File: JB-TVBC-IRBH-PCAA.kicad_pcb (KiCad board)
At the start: 2 copper layers, 65 x 56 mm, 11 parts, among them J1 CONN_2x20_FEM_100PITCH_635INS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, U1 CAT24C32

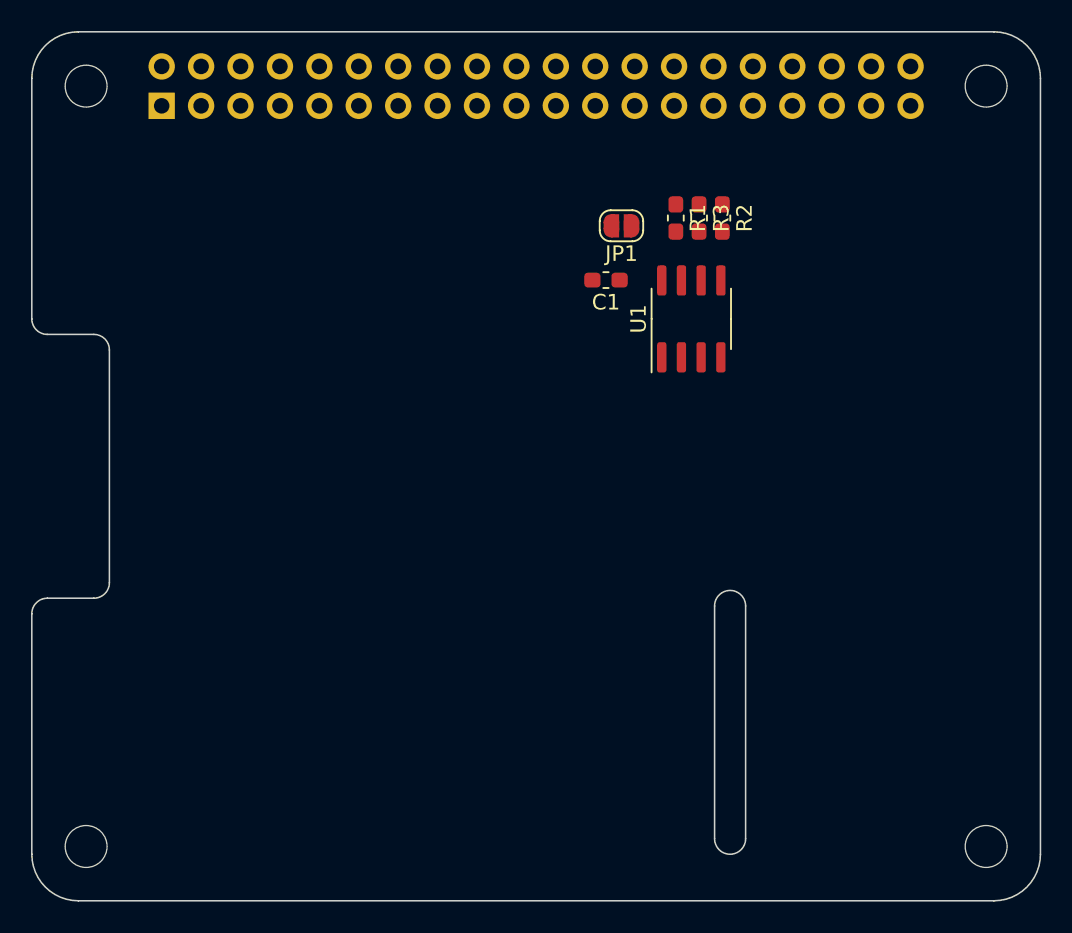
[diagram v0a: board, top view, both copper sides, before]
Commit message: WIP. need to remove pull-up on PHASE and add pull-down on IN (gate driver
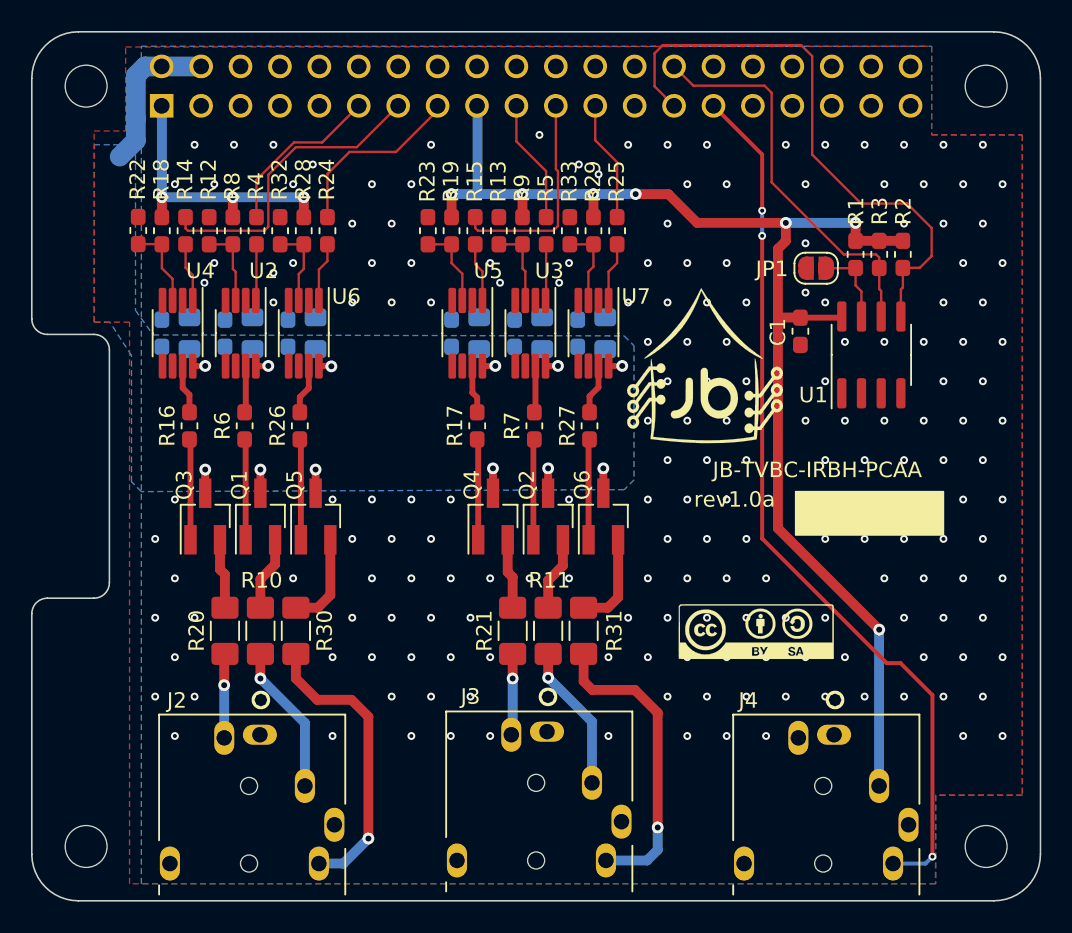
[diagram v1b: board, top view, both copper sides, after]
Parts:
- added C10: 4.7uF_CER_0805_16V, Capacitor_SMD:C_0805_2012Metric_Pad1.15x1.40mm_HandSolder, B.Cu at (118.3, 93.4)
- added C11: 4.7uF_CER_0805_16V, Capacitor_SMD:C_0805_2012Metric_Pad1.15x1.40mm_HandSolder, B.Cu at (137.0, 93.4)
- added C12: 100nF_CER_0603_50V, Capacitor_SMD:C_0603_1608Metric_Pad1.05x0.95mm_HandSolder, B.Cu at (116.5, 93.4)
- added C13: 100nF_CER_0603_50V, Capacitor_SMD:C_0603_1608Metric_Pad1.05x0.95mm_HandSolder, B.Cu at (135.2, 93.4)
- added C2: 4.7uF_CER_0805_16V, Capacitor_SMD:C_0805_2012Metric_Pad1.15x1.40mm_HandSolder, B.Cu at (114.2, 93.4)
- added C3: 4.7uF_CER_0805_16V, Capacitor_SMD:C_0805_2012Metric_Pad1.15x1.40mm_HandSolder, B.Cu at (132.9, 93.4)
- added C4: 100nF_CER_0603_50V, Capacitor_SMD:C_0603_1608Metric_Pad1.05x0.95mm_HandSolder, B.Cu at (112.4, 93.4)
- added C5: 100nF_CER_0603_50V, Capacitor_SMD:C_0603_1608Metric_Pad1.05x0.95mm_HandSolder, B.Cu at (131.1, 93.4)
- added C6: 4.7uF_CER_0805_16V, Capacitor_SMD:C_0805_2012Metric_Pad1.15x1.40mm_HandSolder, B.Cu at (110.2, 93.4)
- added C7: 4.7uF_CER_0805_16V, Capacitor_SMD:C_0805_2012Metric_Pad1.15x1.40mm_HandSolder, B.Cu at (128.8, 93.4)
- added C8: 100nF_CER_0603_50V, Capacitor_SMD:C_0603_1608Metric_Pad1.05x0.95mm_HandSolder, B.Cu at (108.4, 93.4)
- added C9: 100nF_CER_0603_50V, Capacitor_SMD:C_0603_1608Metric_Pad1.05x0.95mm_HandSolder, B.Cu at (127.1, 93.4)
- added G***: LOGO, JB_Bitmaps:CC-BY-SA_10MM, F.Cu at (146.7, 112.6)
- added G***: LOGO, JB_Bitmaps:JB_Logo_10MM, F.Cu at (143.4, 95.5)
- added J2: SJ-435107, JB_Connector_Barrel_Audio:SJ-435107, F.Cu at (114.0, 127.6)
- added J3: SJ-435107, JB_Connector_Barrel_Audio:SJ-435107, F.Cu at (132.5, 127.4)
- added J4: SJ-435107, JB_Connector_Barrel_Audio:SJ-435107, F.Cu at (151.0, 127.6)
- added Q1: DMG2305UX-7, Package_TO_SOT_SMD:SOT-23_Handsoldering, F.Cu at (114.7, 105.2)
- added Q2: DMG2305UX-7, Package_TO_SOT_SMD:SOT-23_Handsoldering, F.Cu at (133.3, 105.2)
- added Q3: DMG2305UX-7, Package_TO_SOT_SMD:SOT-23_Handsoldering, F.Cu at (111.2, 105.2)
- added Q4: DMG2305UX-7, Package_TO_SOT_SMD:SOT-23_Handsoldering, F.Cu at (129.7, 105.2)
- added Q5: DMG2305UX-7, Package_TO_SOT_SMD:SOT-23_Handsoldering, F.Cu at (118.3, 105.2)
- added Q6: DMG2305UX-7, Package_TO_SOT_SMD:SOT-23_Handsoldering, F.Cu at (136.8, 105.2)
- added R10: 137R_1206_250MW, Resistor_SMD:R_1206_3216Metric_Pad1.42x1.75mm_HandSolder, F.Cu at (114.7, 112.6)
- added R11: 137R_1206_250MW, Resistor_SMD:R_1206_3216Metric_Pad1.42x1.75mm_HandSolder, F.Cu at (133.3, 112.6)
- added R12: 0R_0603_100MW, Resistor_SMD:R_0603_1608Metric_Pad1.05x0.95mm_HandSolder, F.Cu at (111.4, 86.8)
- added R13: 0R_0603_100MW, Resistor_SMD:R_0603_1608Metric_Pad1.05x0.95mm_HandSolder, F.Cu at (130.1, 86.8)
- added R14: 0R_0603_100MW, Resistor_SMD:R_0603_1608Metric_Pad1.05x0.95mm_HandSolder, F.Cu at (109.9, 86.8)
- added R15: 0R_0603_100MW, Resistor_SMD:R_0603_1608Metric_Pad1.05x0.95mm_HandSolder, F.Cu at (128.6, 86.8)
- added R16: 0R_0603_100MW, Resistor_SMD:R_0603_1608Metric_Pad1.05x0.95mm_HandSolder, F.Cu at (110.2, 99.4)
- added R17: 0R_0603_100MW, Resistor_SMD:R_0603_1608Metric_Pad1.05x0.95mm_HandSolder, F.Cu at (128.7, 99.4)
- added R18: 0R_0603_100MW, Resistor_SMD:R_0603_1608Metric_Pad1.05x0.95mm_HandSolder, F.Cu at (108.4, 86.8)
- added R19: 0R_0603_100MW, Resistor_SMD:R_0603_1608Metric_Pad1.05x0.95mm_HandSolder, F.Cu at (127.1, 86.8)
- added R20: 137R_1206_250MW, Resistor_SMD:R_1206_3216Metric_Pad1.42x1.75mm_HandSolder, F.Cu at (112.4, 112.6)
- added R21: 137R_1206_250MW, Resistor_SMD:R_1206_3216Metric_Pad1.42x1.75mm_HandSolder, F.Cu at (131.0, 112.6)
- added R22: 0R_0603_100MW, Resistor_SMD:R_0603_1608Metric_Pad1.05x0.95mm_HandSolder, F.Cu at (106.9, 86.8)
- added R23: 0R_0603_100MW, Resistor_SMD:R_0603_1608Metric_Pad1.05x0.95mm_HandSolder, F.Cu at (125.5, 86.8)
- added R24: 0R_0603_100MW, Resistor_SMD:R_0603_1608Metric_Pad1.05x0.95mm_HandSolder, F.Cu at (119.0, 86.8)
- added R25: 0R_0603_100MW, Resistor_SMD:R_0603_1608Metric_Pad1.05x0.95mm_HandSolder, F.Cu at (137.7, 86.8)
- added R26: 0R_0603_100MW, Resistor_SMD:R_0603_1608Metric_Pad1.05x0.95mm_HandSolder, F.Cu at (117.3, 99.4)
- added R27: 0R_0603_100MW, Resistor_SMD:R_0603_1608Metric_Pad1.05x0.95mm_HandSolder, F.Cu at (135.9, 99.4)
- added R28: 0R_0603_100MW, Resistor_SMD:R_0603_1608Metric_Pad1.05x0.95mm_HandSolder, F.Cu at (117.5, 86.8)
- added R29: 0R_0603_100MW, Resistor_SMD:R_0603_1608Metric_Pad1.05x0.95mm_HandSolder, F.Cu at (136.2, 86.8)
- added R30: 137R_1206_250MW, Resistor_SMD:R_1206_3216Metric_Pad1.42x1.75mm_HandSolder, F.Cu at (117.0, 112.6)
- added R31: 137R_1206_250MW, Resistor_SMD:R_1206_3216Metric_Pad1.42x1.75mm_HandSolder, F.Cu at (135.6, 112.6)
- added R32: 0R_0603_100MW, Resistor_SMD:R_0603_1608Metric_Pad1.05x0.95mm_HandSolder, F.Cu at (116.0, 86.8)
- added R33: 0R_0603_100MW, Resistor_SMD:R_0603_1608Metric_Pad1.05x0.95mm_HandSolder, F.Cu at (134.7, 86.8)
- added R4: 0R_0603_100MW, Resistor_SMD:R_0603_1608Metric_Pad1.05x0.95mm_HandSolder, F.Cu at (114.5, 86.8)
- added R5: 0R_0603_100MW, Resistor_SMD:R_0603_1608Metric_Pad1.05x0.95mm_HandSolder, F.Cu at (133.1, 86.8)
- added R6: 0R_0603_100MW, Resistor_SMD:R_0603_1608Metric_Pad1.05x0.95mm_HandSolder, F.Cu at (113.7, 99.4)
- added R7: 0R_0603_100MW, Resistor_SMD:R_0603_1608Metric_Pad1.05x0.95mm_HandSolder, F.Cu at (132.4, 99.4)
- added R8: 0R_0603_100MW, Resistor_SMD:R_0603_1608Metric_Pad1.05x0.95mm_HandSolder, F.Cu at (113.0, 86.8)
- added R9: 0R_0603_100MW, Resistor_SMD:R_0603_1608Metric_Pad1.05x0.95mm_HandSolder, F.Cu at (131.6, 86.8)
- added U2: LTC1693-5, Package_SO:MSOP-8_3x3mm_P0.65mm, F.Cu at (113.5, 93.4)
- added U3: LTC1693-5, Package_SO:MSOP-8_3x3mm_P0.65mm, F.Cu at (132.1, 93.4)
- added U4: LTC1693-5, Package_SO:MSOP-8_3x3mm_P0.65mm, F.Cu at (109.4, 93.4)
- added U5: LTC1693-5, Package_SO:MSOP-8_3x3mm_P0.65mm, F.Cu at (128.1, 93.4)
- added U6: LTC1693-5, Package_SO:MSOP-8_3x3mm_P0.65mm, F.Cu at (117.5, 93.4)
- added U7: LTC1693-5, Package_SO:MSOP-8_3x3mm_P0.65mm, F.Cu at (136.2, 93.4)
- C1: value 100nF_0603_50V -> 100nF_CER_0603_50V
- moved C1 13.0 mm to (149.5, 93.3), turned to 270 degrees
- moved JP1 12.8 mm to (150.5, 89.2)
- moved R2 11.9 mm to (156.1, 88.3)
- moved R3 11.8 mm to (154.6, 88.3)
- moved U1 11.8 mm to (154.1, 94.8)
- moved R1 11.8 mm to (153.1, 88.3)
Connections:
- J1 pad 11: Net-(J1-Pad11) -> /OUT0
- J1 pad 13: Net-(J1-Pad13) -> /OUT1
- J1 pad 15: Net-(J1-Pad15) -> /OUT2
- J1 pad 19: Net-(J1-Pad19) -> /OUT3
- J1 pad 21: Net-(J1-Pad21) -> /OUT4
- J1 pad 23: Net-(J1-Pad23) -> /OUT5
- J1 pad 29: Net-(J1-Pad29) -> /IN0
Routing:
- net +3V3: track 0.00 -> 103.4 mm, vias 0 -> 10
- net /IN0: track 0.00 -> 57.5 mm, vias 0 -> 3
- net /ID_SDA: track 0.00 -> 37.7 mm
- net /ID_SCL: track 0.00 -> 25.6 mm
- net +5V: track 0.00 -> 24.4 mm, vias 0 -> 12
- net /IR_OUT5: track 0.00 -> 19.8 mm, vias 0 -> 1
- net /OUT1: track 0.00 -> 19.8 mm
- net /IR_OUT2: track 0.00 -> 19.0 mm, vias 0 -> 1
- net /OUT4: track 0.00 -> 14.0 mm
- net /OUT2: track 0.00 -> 11.9 mm
- net /OUT0: track 0.00 -> 11.0 mm
- net /IR_OUT0: track 0.00 -> 9.70 mm, vias 0 -> 1
- net /IR_OUT3: track 0.00 -> 9.48 mm, vias 0 -> 1
- net /OUT3: track 0.00 -> 7.97 mm
- net /OUT5: track 0.00 -> 7.76 mm
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- added copper zone on B.Cu, net +5V
- added copper zone on B.Cu, net GND
- added copper zone on F.Cu, net GND
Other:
- outline, holes or cut-outs redrawn
- net class PWR added: clearance 0.1524, trace_width 0.635, via_dia 0.762, via_drill 0.381
- net class SIGNAL added: clearance 0.1524, trace_width 0.1524, via_dia 0.508, via_drill 0.254
- board text added: "JB-TVBC-IRBH-PCAA"
- board text added: "rev1.0a"

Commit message: adding fiducial + graphics symbol
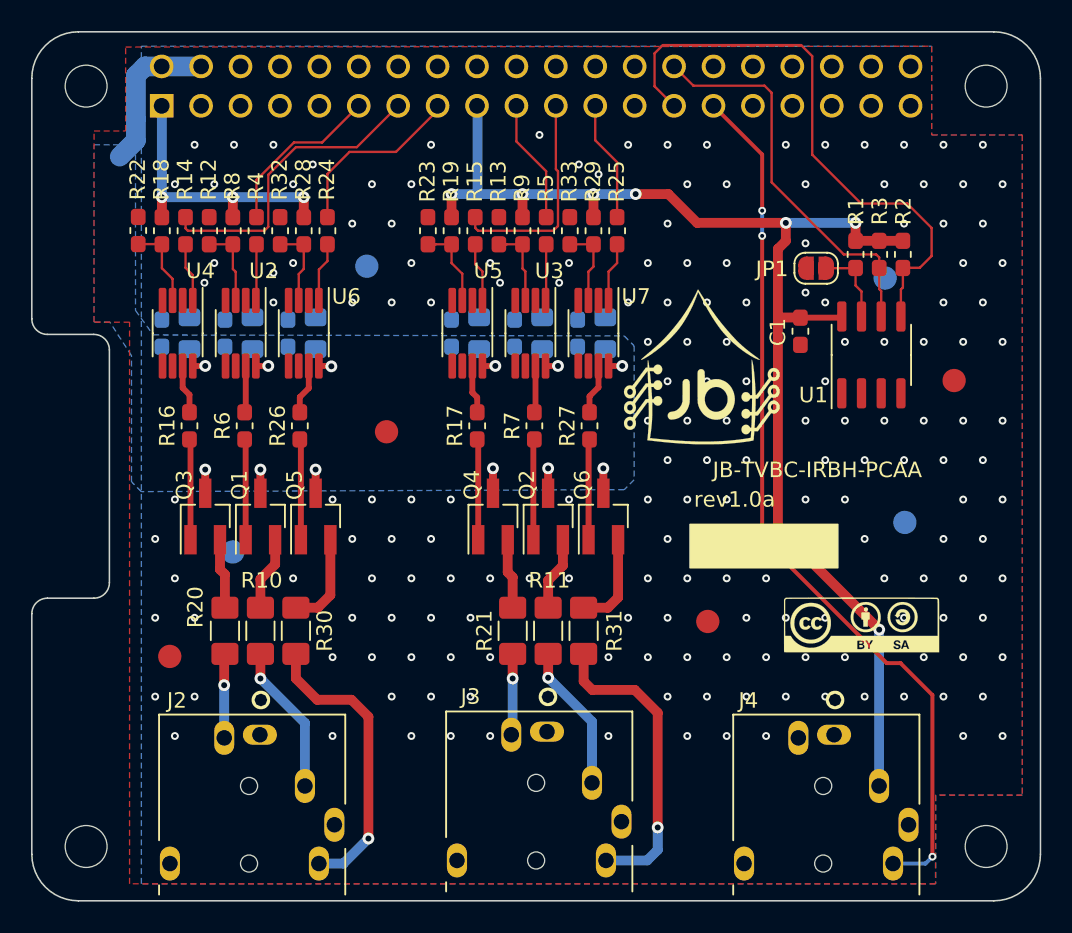
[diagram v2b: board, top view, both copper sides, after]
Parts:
- removed G***: LOGO, JB_Bitmaps:CC-BY-SA_10MM
- removed G***: LOGO, JB_Bitmaps:JB_Logo_10MM
- added FID1: Fiducial, JB_Mechanical:Fiducial_1.5mm_Mask3mm, F.Cu at (122.9, 99.8)
- added FID2: Fiducial, JB_Mechanical:Fiducial_1.5mm_Mask3mm, F.Cu at (108.9, 114.3)
- added FID3: Fiducial, JB_Mechanical:Fiducial_1.5mm_Mask3mm, F.Cu at (143.6, 112.0)
- added FID4: Fiducial, JB_Mechanical:Fiducial_1.5mm_Mask3mm, F.Cu at (159.4, 96.5)
- added FID5: Fiducial, JB_Mechanical:Fiducial_1.5mm_Mask3mm, B.Cu at (121.6, 89.1)
- added FID6: Fiducial, JB_Mechanical:Fiducial_1.5mm_Mask3mm, B.Cu at (155.0, 89.9)
- added FID7: Fiducial, JB_Mechanical:Fiducial_1.5mm_Mask3mm, B.Cu at (113.0, 107.5)
- added FID8: Fiducial, JB_Mechanical:Fiducial_1.5mm_Mask3mm, B.Cu at (156.3, 105.6)
- added G1: JudeBake_Logo, JB_Bitmaps:JB_Logo_10MM, F.Cu at (143.2, 95.6)
- added G2: CC-BY-SA_Logo, JB_Bitmaps:CC-BY-SA_10MM, F.Cu at (153.5, 112.2)
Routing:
- net GND: vias 193 -> 185
